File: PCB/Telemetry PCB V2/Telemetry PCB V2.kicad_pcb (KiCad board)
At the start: 4 copper layers, 70 x 70 mm, 47 parts, among them IC1 E22-900M22S, J1 USB_C_Receptacle_USB2.0_16P, J2 DBG/PGRM Hdr., J3 DATA IN, J4 GPS, J5 Battery, SW1 SW_MEC_5E, SW2 SW_MEC_5E, U1 STM32F411CEUx, U2 MCP1700x-250xxTT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

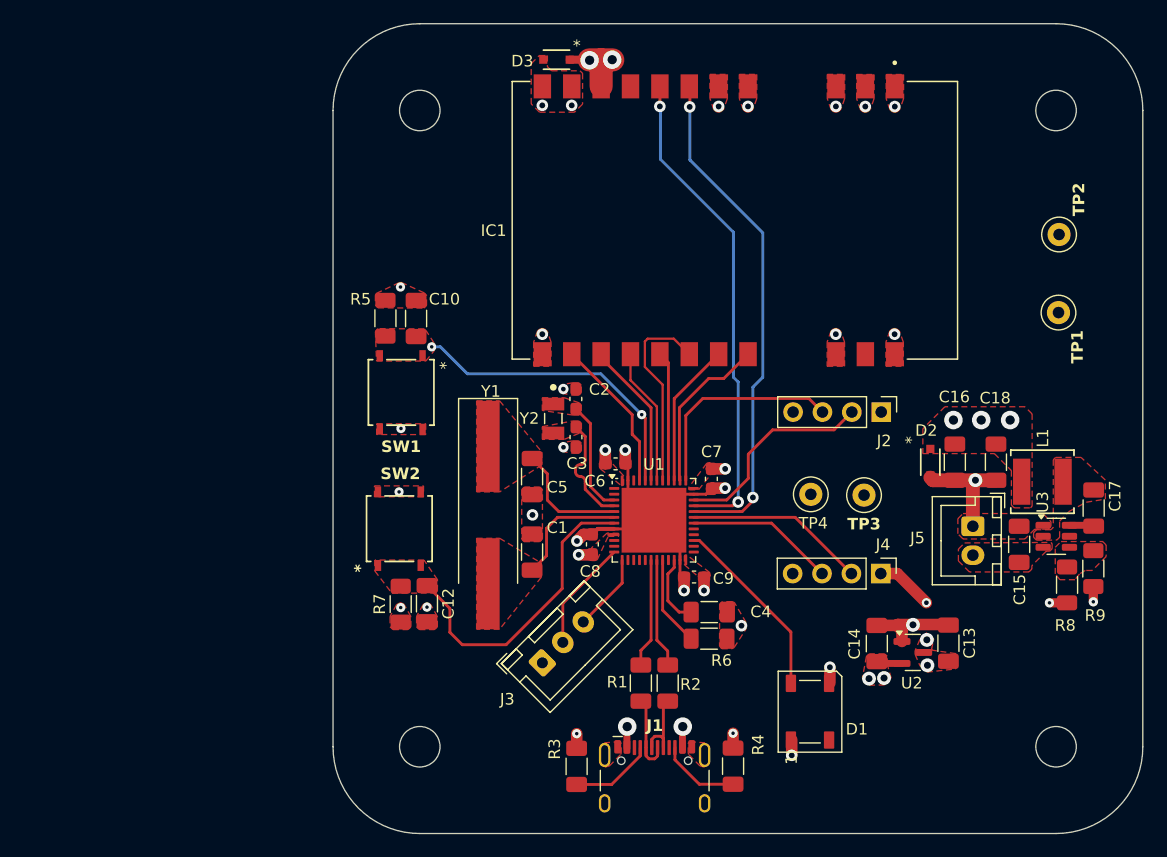
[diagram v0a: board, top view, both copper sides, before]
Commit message: Production files generated
one via and a single silkscreen tweaked to fit jlcpcb rules. All production files generated following jlcpcb guidelines
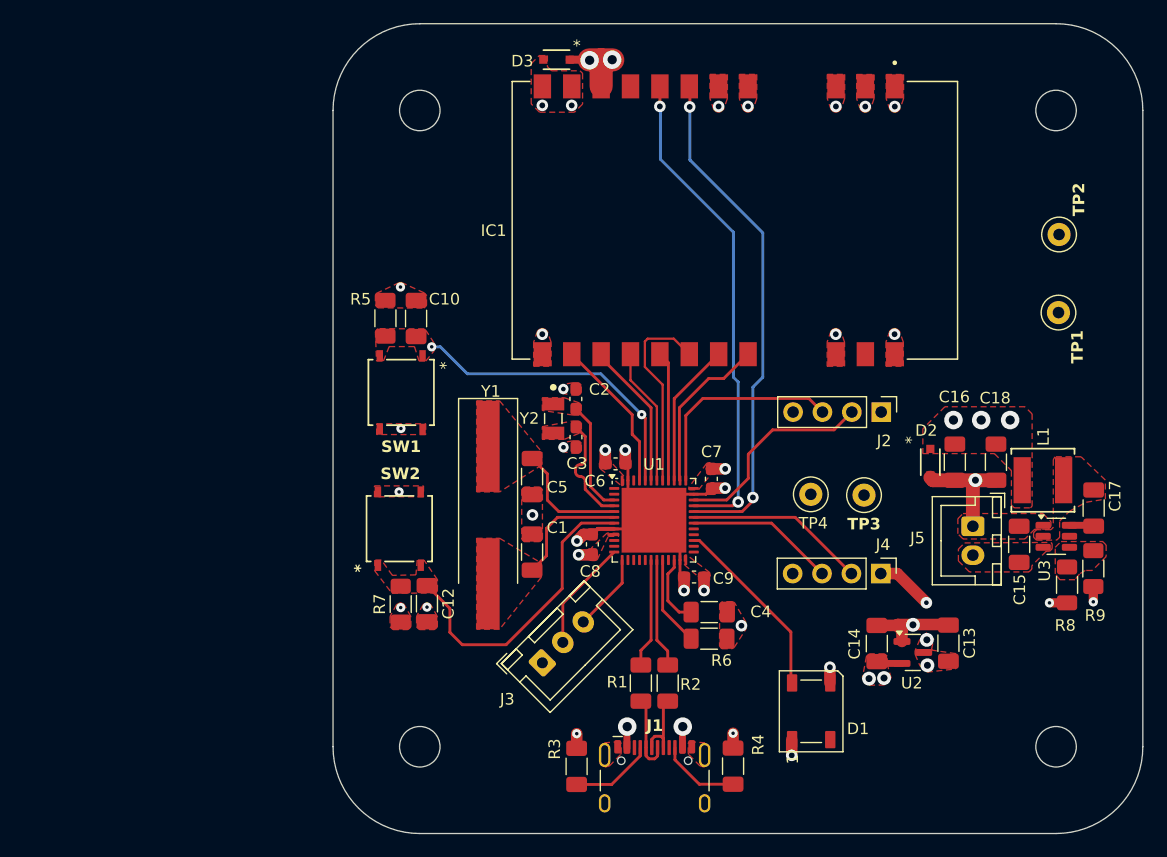
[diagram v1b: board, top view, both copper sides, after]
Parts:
- moved L1 0.14 mm to (184.2, 87.9)
- moved D1 0.11 mm to (164.2, 107.9)
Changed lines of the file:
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@@
 			(plot_on_all_layers_selection 0x0000000_00000000)
 			(disableapertmacros no)
-			(usegerberextensions no)
-			(usegerberattributes yes)
-			(usegerberadvancedattributes yes)
-			(creategerberjobfile yes)
+			(usegerberextensions yes)
+			(usegerberattributes no)
+			(usegerberadvancedattributes no)
+			(creategerberjobfile no)
 			(dashed_line_dash_ratio 12.000000)
 			(dashed_line_gap_ratio 3.000000)
@@
 			(psa4output no)
 			(plotreference yes)
-			(plotvalue yes)
+			(plotvalue no)
 			(plotfptext yes)
 			(plotinvisibletext no)
 			(sketchpadsonfab no)
-			(subtractmaskfromsilk no)
+			(subtractmaskfromsilk yes)
 			(outputformat 1)
 			(mirror no)
@@
 		(at 150.6125 91.36)
 		(descr "QFN, 48 Pin (http://www.st.com/resource/en/datasheet/stm32f042k6.pdf#page=94), generated with kicad-footprint-generator ipc_noLead_generator.py")
-		(tags "QFN NoLead ST_UFQFPN48 Analog_CP-48-13 JEDEC_MO-220-WKKD-4")
+		(tags "QFN NoLead")
 		(property "Reference" "U1"
 			(at 0 -4.83 0)
@@
 	(footprint "SRN5040_3R3M:IND_SRN5040_BRN"
 		(layer "F.Cu")
-		(at 184.188199 88.029601 180)
+		(at 184.2343 87.9 180)
 		(tags "SRN5040-3R3M ")
 		(property "Reference" "L1"
@@
 		(tags "SMD SMT crystal hand-soldering")
 		(property "Reference" "Y1"
-			(at -10.692499 -0.235 360)
+			(at -10.692499 -0.235 0)
 			(layer "F.SilkS")
 			(effects
@@
 		(tags "TSOT TO_SOT_SMD")
 		(property "Reference" "U3"
-			(at -1.1825 -2.949999 90)
+			(at -1.016399 2.9754 -90)
 			(layer "F.SilkS")
 			(effects
@@
 	(footprint "LED_SMD:LED_WS2812B_PLCC4_5.0x5.0mm_P3.2mm"
 		(layer "F.Cu")
-		(at 164.1 107.91 90)
+		(at 164.2 107.875 90)
 		(descr "5.0mm x 5.0mm Addressable RGB LED NeoPixel, https://cdn-shop.adafruit.com/datasheets/WS2812B.pdf")
 		(tags "LED RGB NeoPixel PLCC-4 5050")
@@
 	(via
 		(at 174.16 98.49)
-		(size 0.8)
+		(size 1)
 		(drill 0.4)
 		(layers "F.Cu" "B.Cu")
@@
 	)
 	(zone
+		(net 9)
+		(net_name "BOOT0")
+		(layer "F.Cu")
+		(name "$teardrop_padvia$")
+		(hatch full 0.1)
+		(priority 30002)
+		(attr
+			(teardrop
+				(type padvia)
+			)
+		)
+		(connect_pads yes
+			(clearance 0)
+		)
+		(min_thickness 0.0254)
+		(filled_areas_thickness no)
+		(fill yes
+			(thermal_gap 0.5)
+			(thermal_bridge_width 0.5)
+			(island_removal_mode 1)
+			(island_area_min 10)
+		)
+		(polygon
+			(pts
+				(xy 149.7375 82.900559) (xy 149.9875 82.900559) (xy 149.95 82.23) (xy 149.55 82.229) (xy 149.267157 82.512843)
+			)
+		)
+	)
+	(zone
 		(net 1)
 		(net_name "GND")
@@
 		(filled_areas_thickness no)
 		(fill yes
-			(mode hatch)
 			(thermal_gap 0.5)
 			(thermal_bridge_width 0.5)
-			(hatch_thickness 0.3)
-			(hatch_gap 0.4)
-			(hatch_orientation 0)
-			(hatch_border_algorithm hatch_thickness)
-			(hatch_min_hole_area 0.3)
 		)
 		(polygon
@@
 		(filled_areas_thickness no)
 		(fill yes
-			(mode hatch)
 			(thermal_gap 0.5)
 			(thermal_bridge_width 0.5)
-			(hatch_thickness 0.3)
-			(hatch_gap 0.5)
-			(hatch_orientation 0)
-			(hatch_smoothing_level 1)
-			(hatch_smoothing_value 0.1)
-			(hatch_border_algorithm hatch_thickness)
-			(hatch_min_hole_area 0.3)
 		)
 		(polygon
 			(pts
-				(xy 131.9 96.5) (xy 130.73 94.8) (xy 126.48 94.8) (xy 126.48 95.74) (xy 127.96 97.67) (xy 131.76 97.65)
-				(xy 131.89 97.46)
+				(xy 131.9 96.5) (xy 130.73 94.8) (xy 130.15 94.8) (xy 130.034839 96.084839) (xy 128 96.125) (xy 127.05 94.8)
+				(xy 126.48 94.8) (xy 126.48 95.74) (xy 127.96 97.67) (xy 131.76 97.65) (xy 131.89 97.46)
 			)
 		)
@@
 		(polygon
 			(pts
-				(xy 189.628899 89.535) (xy 189.628899 87.884) (xy 187.528899 85.929601) (xy 185.328899 85.929601)
-				(xy 185.1289 86.129601) (xy 185.128899 91.979601) (xy 184.928899 92.179601) (xy 183.678899 92.179601)
-				(xy 183.428899 92.429601) (xy 183.4289 92.829601) (xy 183.678899 93.079601) (xy 185.428899 93.079601)
-				(xy 185.678899 92.829601) (xy 185.678899 91.429601) (xy 186.528899 90.579601) (xy 187.978899 89.804601)
+				(xy 189.628899 89.535) (xy 189.628899 87.884) (xy 187.528899 85.875) (xy 185.274483 85.875185) (xy 185.1289 86.129601)
+				(xy 185.128899 91.979601) (xy 184.928899 92.179601) (xy 183.678899 92.179601) (xy 183.428899 92.429601)
+				(xy 183.4289 92.829601) (xy 183.678899 93.079601) (xy 185.428899 93.079601) (xy 185.678899 92.829601)
+				(xy 185.678899 91.429601) (xy 186.528899 90.579601) (xy 187.978899 89.804601)
 			)
 		)
@@
 	)
 	(zone
+		(net 20)
+		(net_name "RXEN")
+		(layer "F.Cu")
+		(name "$teardrop_padvia$")
+		(hatch full 0.1)
+		(priority 30001)
+		(attr
+			(teardrop
+				(type padvia)
+			)
+		)
+		(connect_pads yes
+			(clearance 0)
+		)
+		(min_thickness 0.0254)
+		(filled_areas_thickness no)
+		(fill yes
+			(thermal_gap 0.5)
+			(thermal_bridge_width 0.5)
+			(island_removal_mode 1)
+			(island_area_min 10)
+		)
+		(polygon
+			(pts
+				(xy 153.845 54.633978) (xy 153.595 54.633978) (xy 153.23806 55.438658) (xy 153.7 55.631) (xy 154.16194 55.438658)
+			)
+		)
+	)
+	(zone
 		(net 7)
 		(net_name "+3.3V")
@@
 		(filled_areas_thickness no)
 		(fill yes
-			(mode hatch)
 			(thermal_gap 0.25)
 			(thermal_bridge_width 0.5)
-			(hatch_thickness 0.3)
-			(hatch_gap 0.5)
-			(hatch_orientation 0)
-			(hatch_smoothing_level 1)
-			(hatch_smoothing_value 0.1)
-			(hatch_border_algorithm hatch_thickness)
-			(hatch_min_hole_area 0.3)
 		)
 		(polygon
 			(pts
-				(xy 126.53 75.05) (xy 126.63 77.6) (xy 130.89 77.6) (xy 131.61 76.71) (xy 131.6 76.03) (xy 130.95 75.03)
-				(xy 130.74 74.82) (xy 126.75 74.8)
+				(xy 126.53 75.05) (xy 126.63 77.6) (xy 127.225 77.6) (xy 127.725 76.35) (xy 129.909708 76.35) (xy 130.306097 77.596291)
+				(xy 130.89 77.6) (xy 131.61 76.71) (xy 131.6 76.03) (xy 130.95 75.03) (xy 130.74 74.82) (xy 126.75 74.8)
 			)
 		)
@@
 	)
 	(zone
-		(net 9)
-		(net_name "BOOT0")
-		(layer "F.Cu")
-		(name "$teardrop_padvia$")
-		(hatch full 0.1)
-		(priority 30002)
-		(attr
-			(teardrop
-				(type padvia)
-			)
-		)
-		(connect_pads yes
-			(clearance 0)
-		)
-		(min_thickness 0.0254)
-		(filled_areas_thickness no)
-		(fill yes
-			(thermal_gap 0.5)
-			(thermal_bridge_width 0.5)
-			(island_removal_mode 1)
-			(island_area_min 10)
-		)
-		(polygon
-			(pts
-				(xy 149.7375 82.900559) (xy 149.9875 82.900559) (xy 149.95 82.23) (xy 149.55 82.229) (xy 149.267157 82.512843)
-			)
-		)
-	)
-	(zone
 		(net 7)
 		(net_name "+3.3V")
@@
 	)
 	(zone
+		(net 23)
+		(net_name "TXEN")
+		(layer "F.Cu")
+		(name "$teardrop_padvia$")
+		(hatch full 0.1)
+		(priority 30000)
+		(attr
+			(teardrop
+				(type padvia)
+			)
+		)
+		(connect_pads yes
+			(clearance 0)
+		)
+		(min_thickness 0.0254)
+		(filled_areas_thickness no)
+		(fill yes
+			(thermal_gap 0.5)
+			(thermal_bridge_width 0.5)
+			(island_removal_mode 1)
+			(island_area_min 10)
+		)
+		(polygon
+			(pts
+				(xy 151.255 54.591989) (xy 151.005 54.591989) (xy 150.65806 55.398658) (xy 151.12 55.591) (xy 151.58194 55.398658)
+			)
+		)
+	)
+	(zone
 		(net 1)
 		(net_name "GND")
@@
 	)
 	(zone
-		(net 20)
-		(net_name "RXEN")
-		(layer "F.Cu")
-		(name "$teardrop_padvia$")
-		(hatch full 0.1)
-		(priority 30001)
-		(attr
-			(teardrop
-				(type padvia)
-			)
-		)
-		(connect_pads yes
-			(clearance 0)
-		)
-		(min_thickness 0.0254)
-		(filled_areas_thickness no)
-		(fill yes
-			(thermal_gap 0.5)
-			(thermal_bridge_width 0.5)
-			(island_removal_mode 1)
-			(island_area_min 10)
-		)
-		(polygon
-			(pts
-				(xy 153.845 54.633978) (xy 153.595 54.633978) (xy 153.23806 55.438658) (xy 153.7 55.631) (xy 154.16194 55.438658)
-			)
-		)
-	)
-	(zone
 		(net 1)
 		(net_name "GND")
@@
 	)
 	(zone
-		(net 23)
-		(net_name "TXEN")
-		(layer "F.Cu")
-		(name "$teardrop_padvia$")
-		(hatch full 0.1)
-		(priority 30000)
-		(attr
-			(teardrop
-				(type padvia)
-			)
-		)
-		(connect_pads yes
-			(clearance 0)
-		)
-		(min_thickness 0.0254)
-		(filled_areas_thickness no)
-		(fill yes
-			(thermal_gap 0.5)
-			(thermal_bridge_width 0.5)
-			(island_removal_mode 1)
-			(island_area_min 10)
-		)
-		(polygon
-			(pts
-				(xy 151.255 54.591989) (xy 151.005 54.591989) (xy 150.65806 55.398658) (xy 151.12 55.591) (xy 151.58194 55.398658)
-			)
-		)
-	)
-	(zone
 		(net 0)
 		(net_name "")
@@
 	)
 	(zone
-		(net 20)
-		(net_name "RXEN")
+		(net 23)
+		(net_name "TXEN")
 		(layer "B.Cu")
 		(name "$teardrop_padvia$")
 		(hatch full 0.1)
-		(priority 30000)
+		(priority 30001)
 		(attr
 			(teardrop
@@
 		(polygon
 			(pts
-				(xy 153.595 56.626022) (xy 153.845 56.626022) (xy 154.16194 55.821342) (xy 153.7 55.629) (xy 153.23806 55.821342)
+				(xy 151.045 56.580054) (xy 151.295 56.580054) (xy 151.58194 55.781342) (xy 151.12 55.589) (xy 150.65806 55.781342)
 			)
 		)
 	)
 	(zone
-		(net 23)
-		(net_name "TXEN")
+		(net 20)
+		(net_name "RXEN")
 		(layer "B.Cu")
 		(name "$teardrop_padvia$")
 		(hatch full 0.1)
-		(priority 30001)
+		(priority 30000)
 		(attr
 			(teardrop
@@
 		(polygon
 			(pts
-				(xy 151.045 56.580054) (xy 151.295 56.580054) (xy 151.58194 55.781342) (xy 151.12 55.589) (xy 150.65806 55.781342)
+				(xy 153.595 56.626022) (xy 153.845 56.626022) (xy 154.16194 55.821342) (xy 153.7 55.629) (xy 153.23806 55.821342)
 			)
 		)

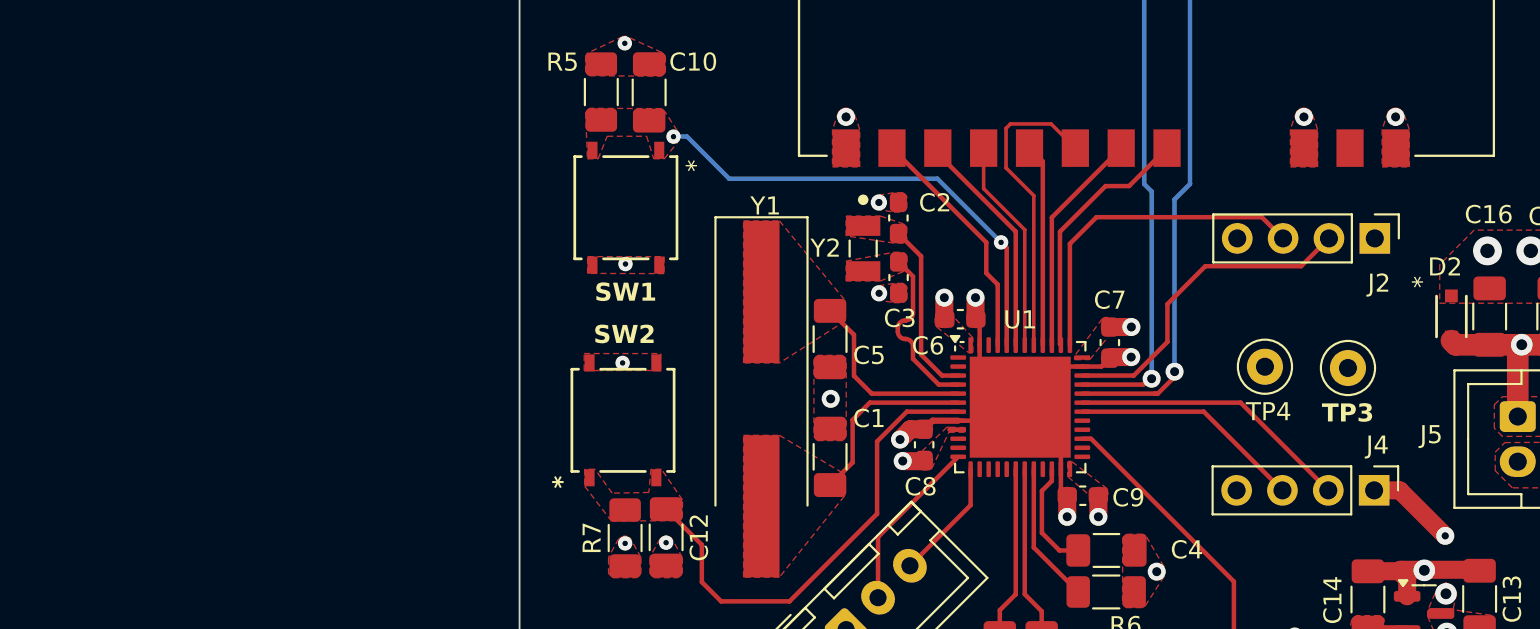
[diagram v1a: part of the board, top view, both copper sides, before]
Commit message: Changed schematic to reflect issues found, started to modify board layout.
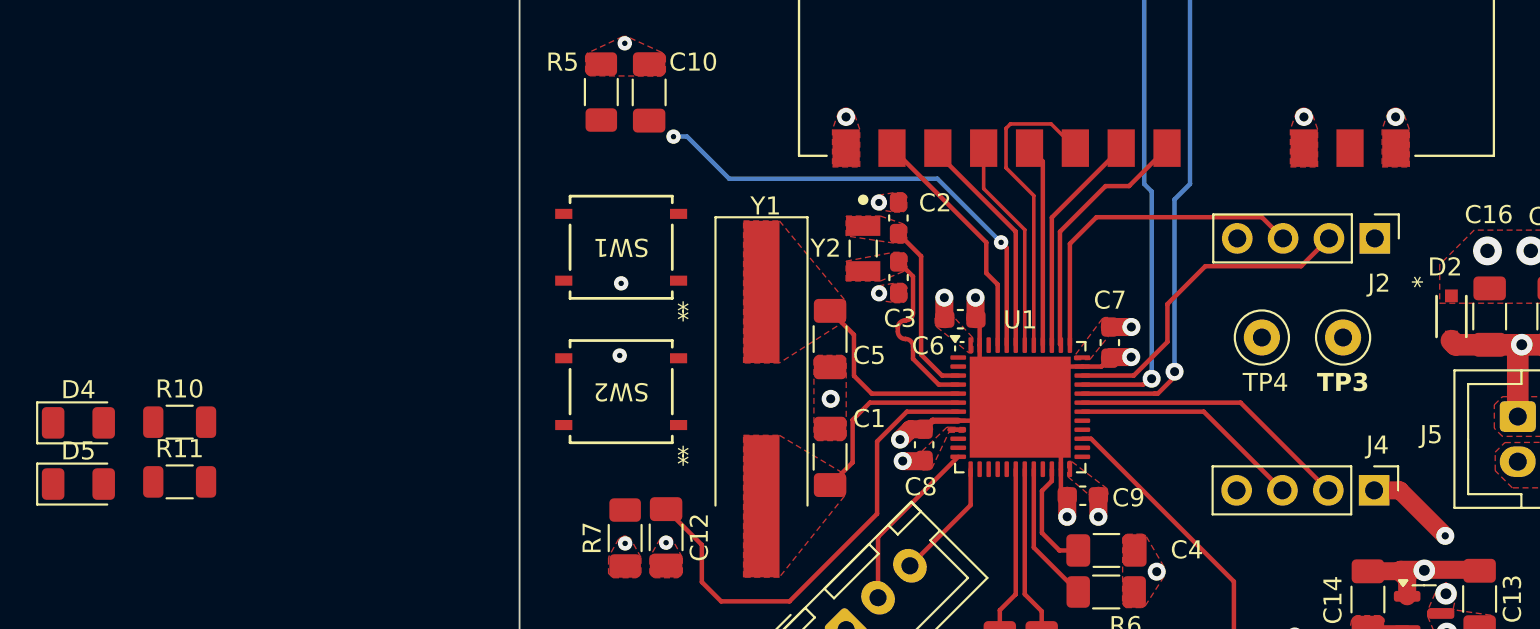
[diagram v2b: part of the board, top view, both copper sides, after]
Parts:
- added D4: GREEN, LED_SMD:LED_1206_3216Metric, F.Cu at (98.4, 92.2)
- added D5: RED, LED_SMD:LED_1206_3216Metric, F.Cu at (98.4, 95.6)
- added R10: 1k, Resistor_SMD:R_1206_3216Metric, F.Cu at (104.0, 92.2)
- added R11: 5.1k, Resistor_SMD:R_1206_3216Metric, F.Cu at (104.0, 95.5)
- moved SW1 2.21 mm to (128.5, 82.5), turned to 180 degrees
- moved TP3 1.71 mm to (168.5, 87.5)
- moved TP4 1.63 mm to (164.0, 87.5)
- moved SW2 1.59 mm to (128.5, 90.5), turned to 180 degrees
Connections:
- R1 pad 1: Net-(U1-PB0) -> Net-(U1-PA11)
- R2 pad 1: Net-(U1-PB1) -> Net-(U1-PA12)
- SW1 pad 1: BOOT0 -> +3.3V
- SW1 pad 2: BOOT0 -> +3.3V
- SW1 pad 3: +3.3V -> BOOT0
- SW1 pad 4: +3.3V -> BOOT0
- U1 pad 18: Net-(U1-PB0) -> unconnected-(U1-PB0-Pad18)
- U1 pad 19: Net-(U1-PB1) -> unconnected-(U1-PB1-Pad19)
- U1 pad 28: unconnected-(U1-PB15-Pad28) -> RXEN
- U1 pad 29: unconnected-(U1-PA8-Pad29) -> TXEN
- U1 pad 32: RXEN -> Net-(U1-PA11)
- U1 pad 33: TXEN -> Net-(U1-PA12)
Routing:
- net (no net): track 0.00 -> 18.9 mm
- net Net-(U1-PB1): track 9.47 -> 0.00 mm
- net Net-(U1-PB0): track 9.44 -> 0.00 mm
- removed copper zone on F.Cu, net BOOT0
- removed copper zone on F.Cu, net NRST
